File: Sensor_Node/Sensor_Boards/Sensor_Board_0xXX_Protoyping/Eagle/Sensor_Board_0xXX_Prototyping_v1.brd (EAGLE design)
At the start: 55 x 35 mm, 24 parts, among them J1 M04_SMD_90, J4 ARDUINO_ISP, U2 ATMEGA328P_TQFP, Y1 8MHZ

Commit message: Finished SensorBoard Prototype
- minor changes
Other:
- board text added: "A/S SensModule Prototyping"
- board text added: "ADC6"
- board text added: "ADC7"
- board text added: "INT0"
- board text added: "INT1"
- board text added: "PC0"
- board text added: "PC1"
- board text added: "PC2"
- board text added: "SCL"
- board text added: "SDA"
- board text removed: "A/S Prototyping"
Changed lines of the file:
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@@
 <setting verticaltext="up"/>
 </settings>
-<grid distance="0.1" unitdist="inch" unit="inch" style="lines" multiple="1" display="yes" altdistance="0.0196850394" altunitdist="inch" altunit="inch"/>
+<grid distance="0.05" unitdist="inch" unit="inch" style="lines" multiple="1" display="yes" altdistance="0.0196850394" altunitdist="inch" altunit="inch"/>
 <layers>
 <layer number="1" name="Top" color="4" fill="1" visible="yes" active="yes"/>
@@
 <text x="48.895" y="11.7475" size="0.8128" layer="21">RX</text>
 <text x="50.8" y="11.7475" size="0.8128" layer="21">GND</text>
-<text x="4.445" y="2.8575" size="1.778" layer="21">A/S
-Prototyping</text>
+<text x="2.413" y="1.3335" size="1.778" layer="21">A/S SensModule Prototyping</text>
 <circle x="40.9575" y="30.48" radius="0.3175" width="0.4064" layer="21"/>
 <text x="53.34" y="33.655" size="0.8128" layer="21" rot="R180">GND</text>
 <circle x="52.3875" y="30.7975" radius="1.27" width="0.4064" layer="21"/>
+<text x="1.27" y="5.461" size="0.8128" layer="21">INT0</text>
+<text x="4.191" y="5.461" size="0.8128" layer="21">SCL</text>
+<text x="6.604" y="5.461" size="0.8128" layer="21">SDA</text>
+<text x="9.144" y="5.461" size="0.8128" layer="21">PC2</text>
+<text x="11.684" y="5.461" size="0.8128" layer="21">PC1</text>
+<text x="16.51" y="5.461" size="0.8128" layer="21">INT1</text>
+<text x="19.431" y="5.588" size="0.6096" layer="21">ADC7</text>
+<text x="21.844" y="5.588" size="0.6096" layer="21">ADC6</text>
+<text x="14.097" y="5.461" size="0.8128" layer="21">PC0</text>
+<wire x1="21.59" y1="33.655" x2="21.59" y2="9.525" width="0.4064" layer="21"/>
+<wire x1="21.59" y1="9.525" x2="20.955" y2="8.89" width="0.4064" layer="21" curve="-90"/>
+<wire x1="20.955" y1="8.89" x2="1.905" y2="8.89" width="0.4064" layer="21"/>
+<wire x1="1.905" y1="8.89" x2="1.27" y2="9.525" width="0.4064" layer="21" curve="-90"/>
+<wire x1="1.27" y1="9.525" x2="1.27" y2="33.655" width="0.4064" layer="21"/>
 </plain>
 <attributes>
@@
 </board>
 </drawing>
-<compatibility>
-<note version="6.3" minversion="6.2.2" severity="warning">
-Since Version 6.2.2 text objects can contain more than one line,
-which will not be processed correctly with this version.
-</note>
-</compatibility>
 </eagle>

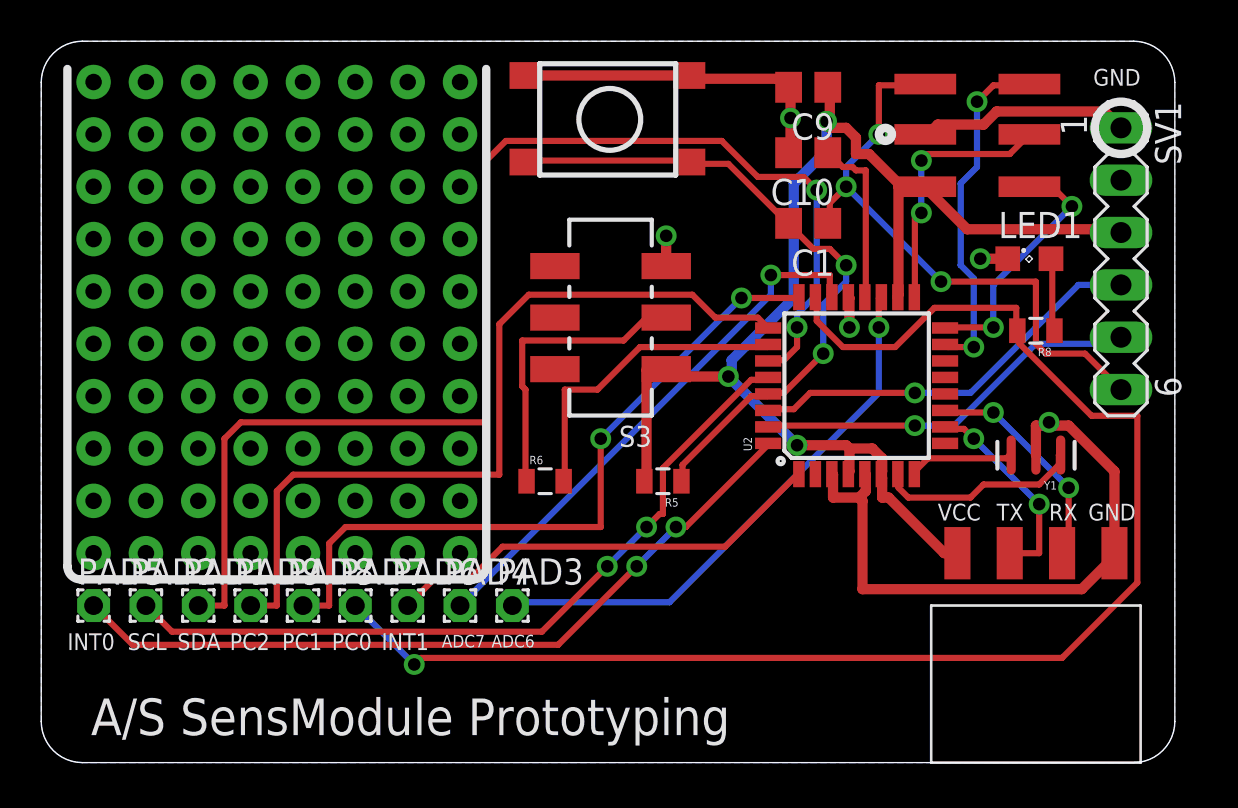
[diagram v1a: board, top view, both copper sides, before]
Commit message: Changes on Sensor Modules
- Finished SensModule-Prototype
- Changed some pin-descriptions on SensModule CO2
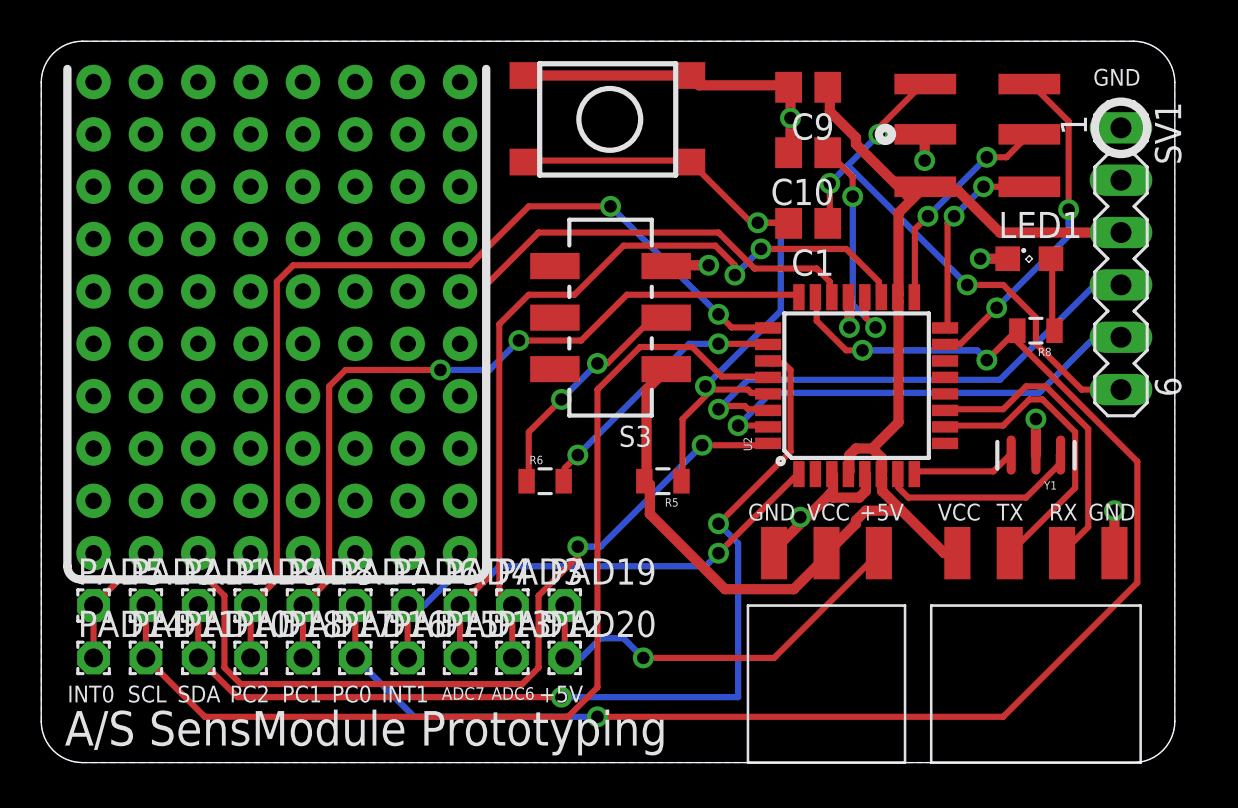
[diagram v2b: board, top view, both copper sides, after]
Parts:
- added PAD10, PAD11, PAD12, PAD13, PAD14, PAD15, PAD16, PAD17, PAD18, PAD19, PAD20: (no value), wirepad:1,6/0,9
- added U$2: M03_SMD_90, myownthings:M03_SMD_90
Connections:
- new net +5V: PAD19.1, PAD20.1, U$2.3
- net ADC6: now also PAD12.1
- net ADC7: now also PAD13.1
- net GND: now also U$2.1
- net INT0: now also PAD14.1
- net INT1: now also PAD15.1
- net L1: now also PAD16.1
- net PC1: now also PAD17.1
- net PC2: now also PAD18.1
- net SCL: now also PAD11.1
- net SDA: now also PAD10.1
- net VCC: now also U$2.2
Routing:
- net GND: track 62.4 -> 34.3 mm, vias 5 -> 8
- net +5V: track 0.00 -> 20.7 mm, vias 0 -> 1
- net SDA: track 62.2 -> 48.5 mm
- net SCL: track 37.2 -> 50.4 mm, vias 2 -> 0
- net ADC6: track 26.8 -> 39.3 mm, vias 1 -> 2
- net ADC7: track 26.2 -> 38.1 mm, vias 1 -> 0
- net INT0: track 37.6 -> 47.1 mm
- net PC2: track 39.6 -> 46.6 mm, vias 0 -> 2
- net FTDI_RXI: track 19.6 -> 24.6 mm
- net MCU_TXO: track 9.92 -> 14.7 mm, vias 2 -> 0
- net PC1: track 34.5 -> 38.4 mm
- net MCU_RXI: track 11.0 -> 14.8 mm, vias 2 -> 0
- net FTDI_TXO: track 18.9 -> 21.8 mm
- net N$3: track 14.4 -> 11.5 mm, vias 0 -> 2
- net N$15: track 8.35 -> 11.1 mm, vias 0 -> 2
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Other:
- board text added: "+5V"

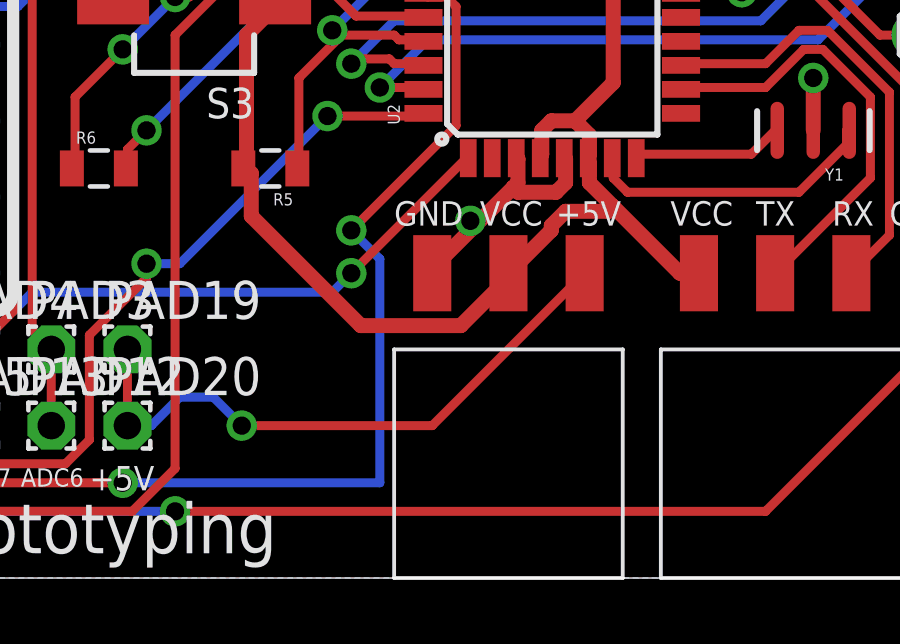
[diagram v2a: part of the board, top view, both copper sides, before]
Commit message: Removed gap between connectors to commBoard
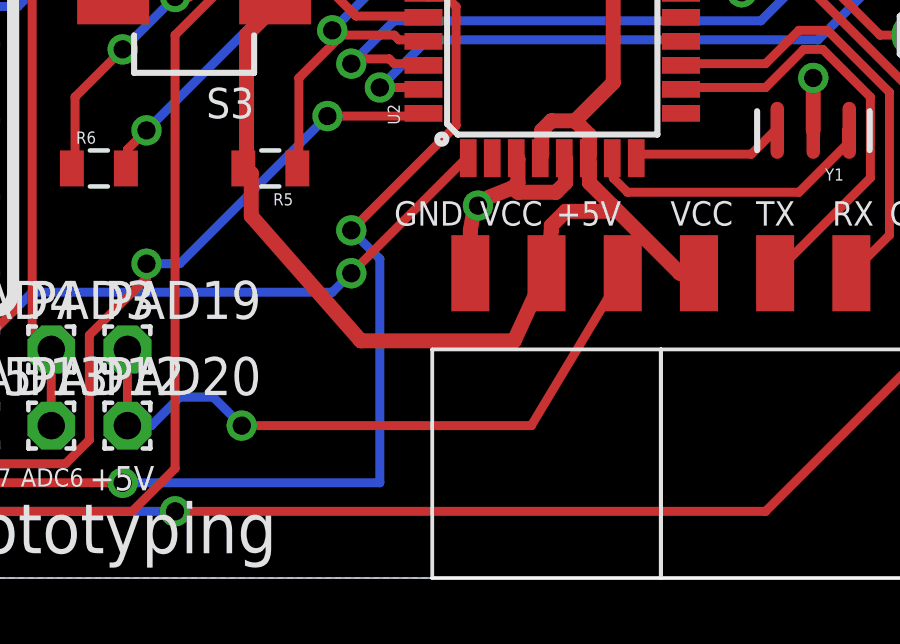
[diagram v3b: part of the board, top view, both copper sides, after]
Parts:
- moved U$2 1.27 mm to (36.8, 10.2)
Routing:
- net +5V: track 20.7 -> 22.7 mm
- net VCC: track 64.5 -> 66.4 mm
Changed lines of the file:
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@@
 <?xml version="1.0" encoding="utf-8"?>
 <!DOCTYPE eagle SYSTEM "eagle.dtd">
-<eagle version="8.2.0">
+<eagle version="8.2.2">
 <drawing>
 <settings>
@@
 <element name="PAD17" library="wirepad" package="1,6/0,9" value="" x="12.7" y="5.08"/>
 <element name="PAD18" library="wirepad" package="1,6/0,9" value="" x="10.16" y="5.08"/>
-<element name="U$2" library="myownthings" package="M03_SMD_90" value="M03_SMD_90" x="35.56" y="10.16"/>
+<element name="U$2" library="myownthings" package="M03_SMD_90" value="M03_SMD_90" x="36.83" y="10.16"/>
 <element name="PAD19" library="wirepad" package="1,6/0,9" value="" x="25.4" y="7.62"/>
 <element name="PAD20" library="wirepad" package="1,6/0,9" value="" x="25.4" y="5.08"/>
@@
 <wire x1="31.59125" y1="33.17875" x2="31.445" y2="33.3375" width="0.5" layer="1"/>
 <wire x1="38.4175" y1="13.17625" x2="38.4175" y2="13.97" width="0.5" layer="1"/>
-<wire x1="35.56" y1="10.31875" x2="36.98875" y2="11.7475" width="0.5" layer="1"/>
-<wire x1="36.98875" y1="11.7475" x2="38.25875" y2="13.0175" width="0.5" layer="1"/>
+<wire x1="36.83" y1="11.58875" x2="36.98875" y2="12.5095" width="0.5" layer="1"/>
+<wire x1="36.98875" y1="12.5095" x2="38.25875" y2="13.0175" width="0.5" layer="1"/>
 <wire x1="38.25875" y1="13.0175" x2="38.4175" y2="13.17625" width="0.5" layer="1"/>
-<wire x1="35.56" y1="10.16" x2="35.56" y2="10.31875" width="0.5" layer="1"/>
+<wire x1="36.83" y1="10.16" x2="36.83" y2="11.58875" width="0.5" layer="1"/>
 <wire x1="38.4175" y1="13.97" x2="38.3605" y2="13.9954" width="0.5" layer="1"/>
 <wire x1="40.005" y1="13.17625" x2="40.005" y2="13.97" width="0.5" layer="1"/>
@@
 <wire x1="42.8625" y1="29.21" x2="42.8625" y2="30.48" width="0.5" layer="1"/>
 <wire x1="42.8625" y1="30.48" x2="42.8925" y2="30.48" width="0.5" layer="1"/>
-<wire x1="36.83" y1="11.90625" x2="36.98875" y2="11.7475" width="0.5" layer="1"/>
+<wire x1="37.084" y1="12.41425" x2="36.98875" y2="12.5095" width="0.5" layer="1"/>
 <via x="45.56125" y="24.4475" extent="1-16" drill="0.6096"/>
 <via x="39.21125" y="21.11375" extent="1-16" drill="0.6096"/>
@@
 <via x="52.07" y="12.22375" extent="1-16" drill="0.6096"/>
 <via x="42.8625" y="29.21" extent="1-16" drill="0.6096"/>
-<via x="36.83" y="11.90625" extent="1-16" drill="0.6096"/>
+<via x="37.084" y="12.41425" extent="1-16" drill="0.6096"/>
 <via x="36.35375" y="31.27375" extent="1-16" drill="0.6096"/>
 </signal>
@@
 <wire x1="44.45" y1="10.16" x2="43.815" y2="10.16" width="0.5" layer="1"/>
 <wire x1="40.79875" y1="13.81125" x2="40.7605" y2="13.9954" width="0.5" layer="1"/>
-<wire x1="39.52875" y1="11.58875" x2="38.1" y2="10.16" width="0.5" layer="1"/>
+<wire x1="39.52875" y1="11.58875" x2="39.37" y2="10.16" width="0.5" layer="1"/>
 <wire x1="39.52875" y1="11.7475" x2="39.52875" y2="11.58875" width="0.5" layer="1"/>
 <wire x1="40.005" y1="12.22375" x2="39.52875" y2="11.7475" width="0.5" layer="1"/>
@@
 <wire x1="41.43375" y1="12.22375" x2="41.5925" y2="12.3825" width="0.5" layer="1"/>
 <wire x1="29.5275" y1="12.065" x2="29.5275" y2="13.49375" width="0.5" layer="1"/>
-<wire x1="33.17875" y1="8.41375" x2="29.5275" y2="12.065" width="0.5" layer="1"/>
-<wire x1="36.5125" y1="8.41375" x2="33.17875" y2="8.41375" width="0.5" layer="1"/>
-<wire x1="38.1" y1="10.00125" x2="36.5125" y2="8.41375" width="0.5" layer="1"/>
+<wire x1="33.17875" y1="7.90575" x2="29.5275" y2="12.065" width="0.5" layer="1"/>
+<wire x1="38.2905" y1="7.90575" x2="33.17875" y2="7.90575" width="0.5" layer="1"/>
+<wire x1="39.37" y1="10.25525" x2="38.2905" y2="7.90575" width="0.5" layer="1"/>
 <wire x1="29.5275" y1="13.49375" x2="29.2625" y2="13.6525" width="0.5" layer="1"/>
-<wire x1="38.1" y1="10.00125" x2="38.1" y2="10.16" width="0.5" layer="1"/>
+<wire x1="39.37" y1="10.25525" x2="39.37" y2="10.16" width="0.5" layer="1"/>
 <wire x1="41.5925" y1="16.51" x2="41.5925" y2="22.38375" width="0.5" layer="1"/>
 <wire x1="40.3225" y1="15.24" x2="41.5925" y2="16.51" width="0.5" layer="1"/>
@@
 <contactref element="U$2" pad="3"/>
 <contactref element="PAD20" pad="1"/>
-<wire x1="35.56" y1="5.08" x2="40.64" y2="10.16" width="0.3" layer="1"/>
-<wire x1="29.21" y1="5.08" x2="35.56" y2="5.08" width="0.3" layer="1"/>
+<wire x1="38.862" y1="5.08" x2="41.91" y2="10.16" width="0.3" layer="1"/>
+<wire x1="29.21" y1="5.08" x2="38.862" y2="5.08" width="0.3" layer="1"/>
 <wire x1="28.2575" y1="6.0325" x2="29.21" y2="5.08" width="0.3" layer="16"/>
 <wire x1="27.14625" y1="6.0325" x2="28.2575" y2="6.0325" width="0.3" layer="16"/>

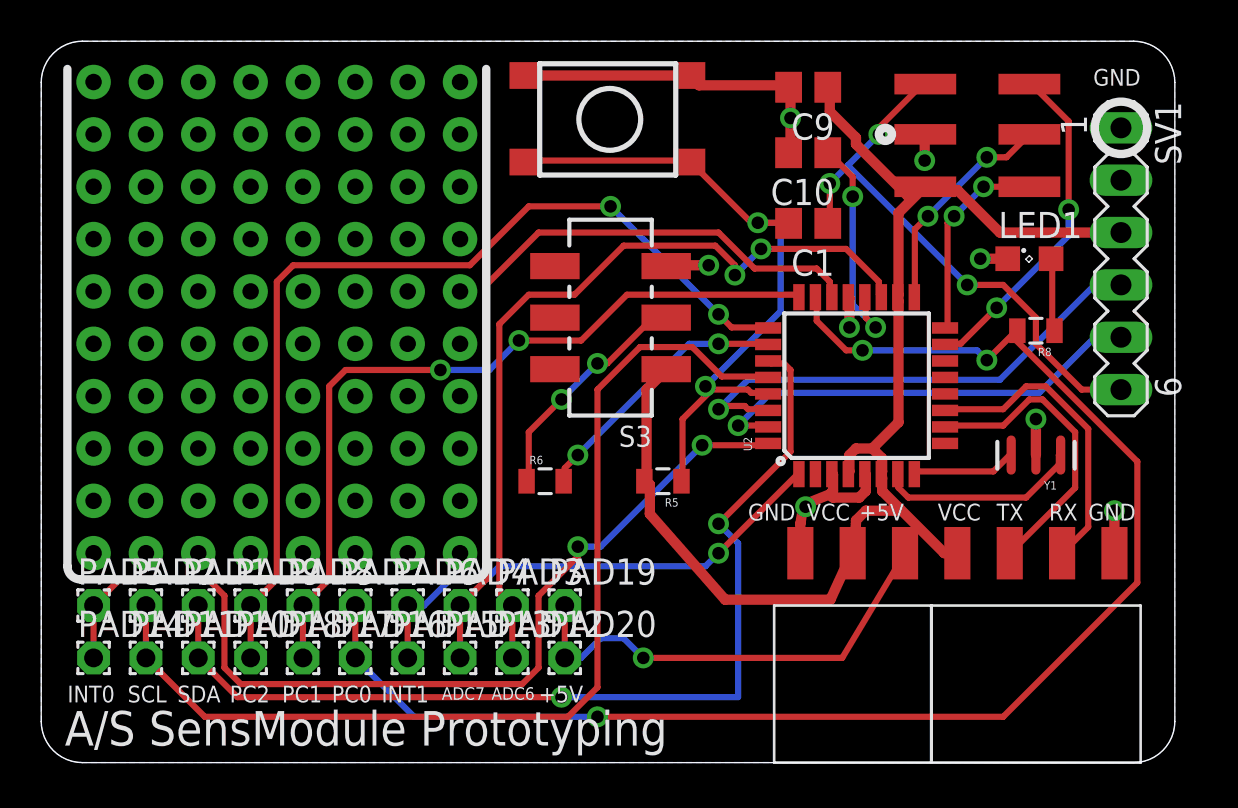
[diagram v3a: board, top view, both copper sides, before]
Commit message: Prototype - Board
- reset path
- minor changes
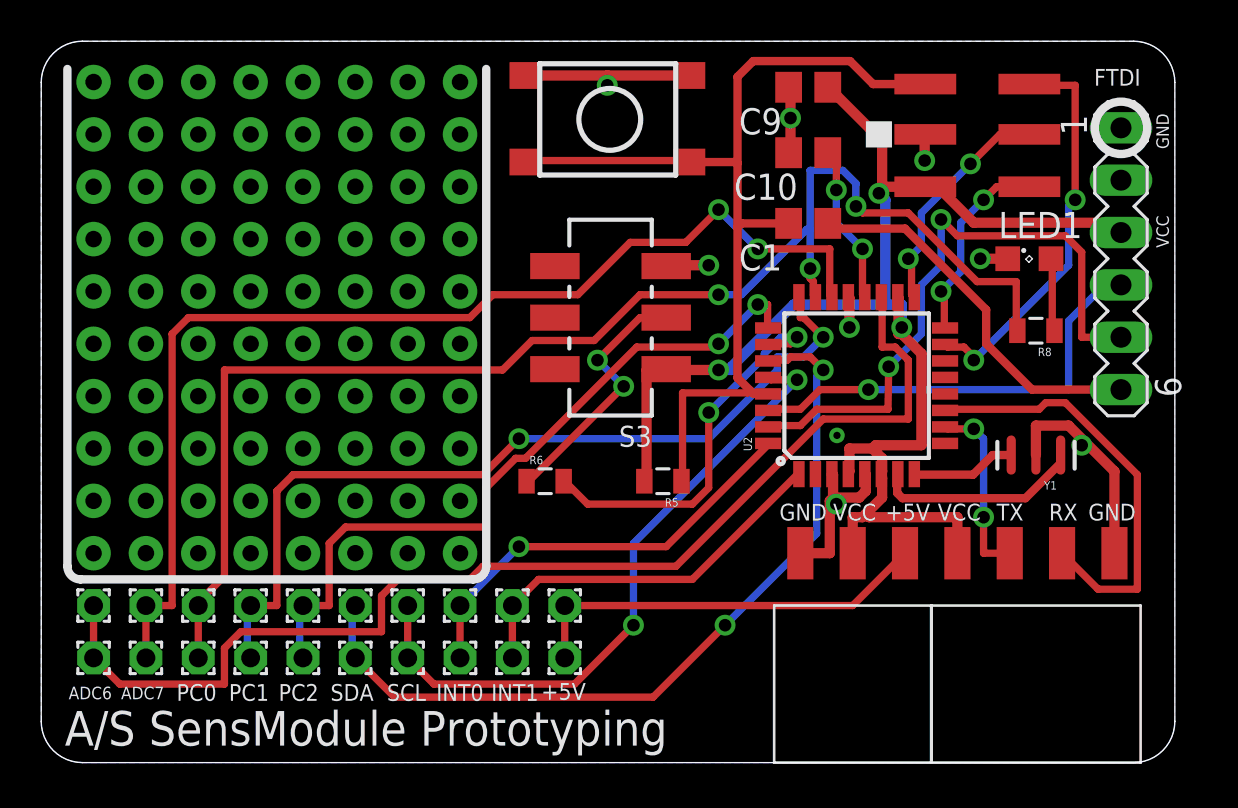
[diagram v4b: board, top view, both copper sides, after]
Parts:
- moved PAD12 20.5 mm to (2.54, 7.62), turned to 180 degrees
- moved PAD3 20.5 mm to (2.54, 5.08), turned to 180 degrees
- moved PAD14 18.0 mm to (20.3, 7.62), turned to 180 degrees
- moved PAD5 18.0 mm to (20.3, 5.08), turned to 180 degrees
- moved PAD13 15.5 mm to (5.08, 7.62), turned to 180 degrees
- moved PAD4 15.5 mm to (5.08, 5.08), turned to 180 degrees
- moved PAD11 13.0 mm to (17.8, 7.62), turned to 180 degrees
- moved PAD2 13.0 mm to (17.8, 5.08), turned to 180 degrees
- moved PAD1 8.03 mm to (15.2, 5.08), turned to 180 degrees
- moved PAD10 8.03 mm to (15.2, 7.62), turned to 180 degrees
- moved PAD16 8.03 mm to (7.62, 7.62), turned to 180 degrees
- moved PAD7 8.03 mm to (7.62, 5.08), turned to 180 degrees
- moved PAD15 5.68 mm to (22.9, 7.62), turned to 180 degrees
- moved PAD6 5.68 mm to (22.9, 5.08), turned to 180 degrees
- moved PAD17 3.59 mm to (10.2, 7.62), turned to 180 degrees
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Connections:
- removed net N$4: C1.2, R5.1, S1.3, S1.4, U2.29
- new net FTDI_RESET: C1.1, SV1.6
- net RESET: now also C1.2, R5.1, S1.3, S1.4, U2.29; no longer C1.1, SV1.6
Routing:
- net N$4: track 32.9 -> 0.00 mm, vias 2 -> 0
- net INT0: track 47.1 -> 20.8 mm, vias 2 -> 1
- net RESET: track 27.4 -> 46.9 mm, vias 3 -> 0
- net SCL: track 50.4 -> 31.8 mm, vias 0 -> 2
- net FTDI_RESET: track 0.00 -> 18.5 mm
- net ADC6: track 39.3 -> 56.8 mm, vias 2 -> 0
- net ADC7: track 38.1 -> 54.6 mm, vias 0 -> 2
- net PC2: track 46.6 -> 35.3 mm
- net SDA: track 48.5 -> 40.2 mm
- net FTDI_TXO: track 21.8 -> 29.9 mm, vias 1 -> 2
- net MCU_RXI: track 14.8 -> 20.8 mm
- net DBG_ENABLE: track 13.1 -> 18.9 mm
- net MCU_TXO: track 14.7 -> 8.92 mm, vias 0 -> 2
- net INT1: track 24.2 -> 19.1 mm, vias 1 -> 0
- net L1: track 71.4 -> 67.3 mm
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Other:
- board text added: "FTDI"
